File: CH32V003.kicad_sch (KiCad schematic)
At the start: 12 parts, among them J7 Program, SW1 SW_SPST, U4 CH32V003FxPx, X1 X322525MOB4SI

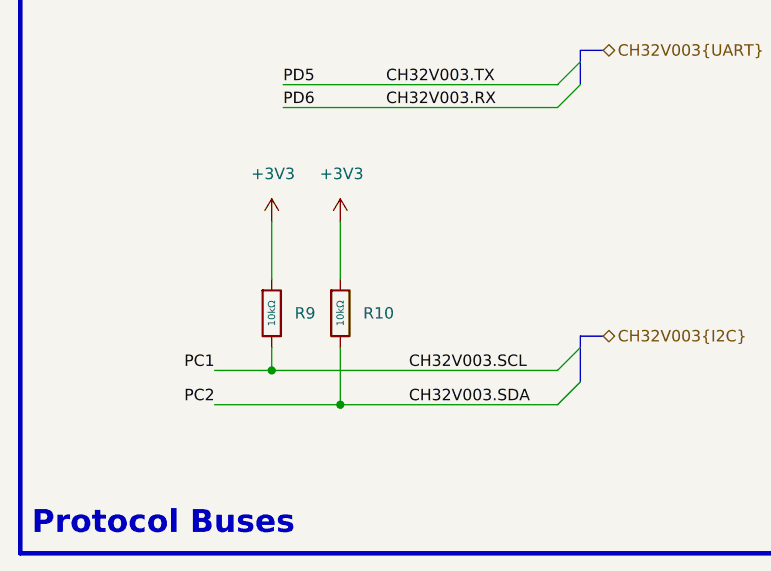
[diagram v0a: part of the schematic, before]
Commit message: finished routing and exported gerber
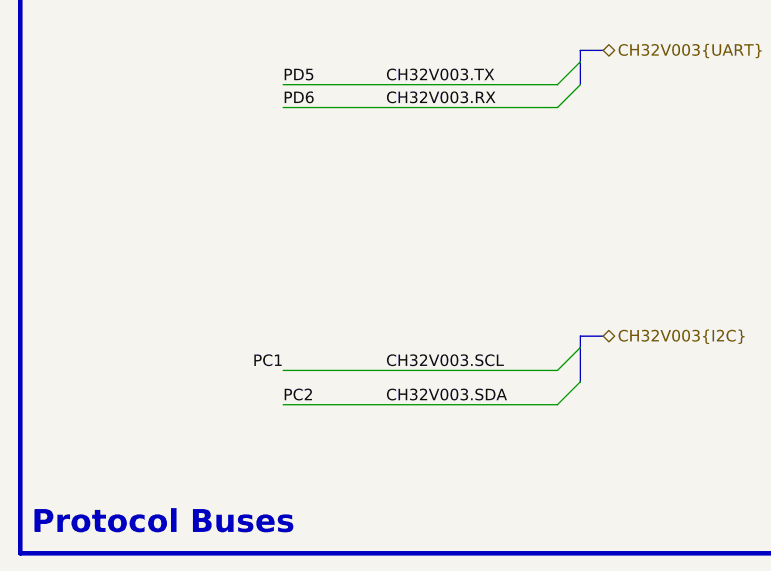
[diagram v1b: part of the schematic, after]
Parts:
- removed R10, R9: 10kΩ, PCM_JLCPCB:R_0402, symbol PCM_JLCPCB-Resistors:0402,10kΩ
